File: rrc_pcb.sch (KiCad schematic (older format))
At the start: 10 parts, among them J1 Voltage Regulator Input, U1 ADXL357Z, U2 Teensy3.6-teensy, U3 BN220-GPS, U4 MS5611

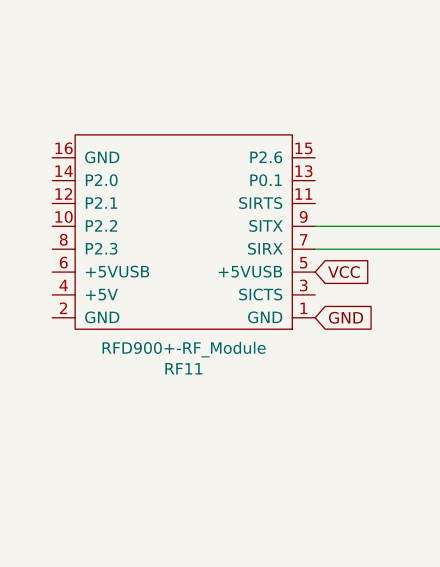
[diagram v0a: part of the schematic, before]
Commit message: added rfd v5-vusb jumper
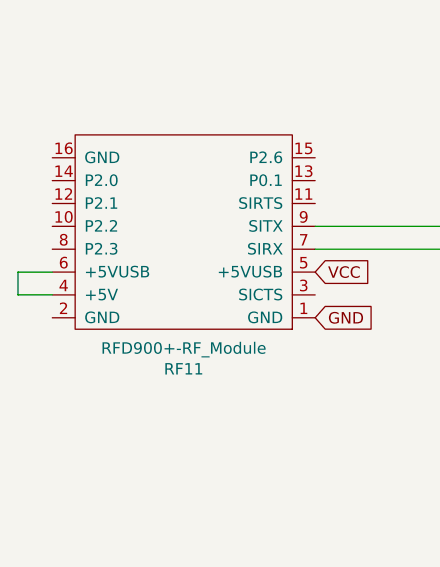
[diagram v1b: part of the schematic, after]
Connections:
- wire segments 38 -> 41
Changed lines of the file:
@@
 Wire Wire Line
 	10150 4900 10150 5300
+Wire Wire Line
+	1800 4600 1650 4600
+Wire Wire Line
+	1650 4600 1650 4500
+Wire Wire Line
+	1650 4500 1800 4500
 $EndSCHEMATC

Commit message: AC_added cool RRC logo
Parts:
- added U5: logo, logo:RRC_logo, symbol rrc_pcb-rescue:logo
- J1: symbol Connector:Conn_01x02_Male -> rrc_pcb-rescue:Conn_01x02_Male-Connector
- R1, R2, R3, R4: symbol Device:R -> rrc_pcb-rescue:R-Device
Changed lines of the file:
@@
 $EndComp
 $Comp
-L Device:R R4
+L rrc_pcb-rescue:R-Device R4
 U 1 1 60F41F75
 P 3200 2600
@@
 $EndComp
 $Comp
-L Device:R R3
+L rrc_pcb-rescue:R-Device R3
 U 1 1 60F426BB
 P 3200 2700
@@
 $EndComp
 $Comp
-L Device:R R1
+L rrc_pcb-rescue:R-Device R1
 U 1 1 60F42E96
 P 7800 4600
@@
 $EndComp
 $Comp
-L Device:R R2
+L rrc_pcb-rescue:R-Device R2
 U 1 1 60F4361A
 P 7800 5000
@@
 $EndComp
 $Comp
-L power:+5V #PWR01
+L rrc_pcb-rescue:+5V-power #PWR01
 U 1 1 60F4946E
 P 8700 1700
@@
 $EndComp
 $Comp
-L power:GND #PWR02
+L rrc_pcb-rescue:GND-power #PWR02
 U 1 1 60F49AB9
 P 8700 1800
@@
 $EndComp
 $Comp
-L Connector:Conn_01x02_Male J1
+L rrc_pcb-rescue:Conn_01x02_Male-Connector J1
 U 1 1 60F4B4B7
 P 8350 1700
@@
 Wire Wire Line
 	1650 4500 1800 4500
+$Comp
+L rrc_pcb-rescue:logo U5
+U 1 1 60F65807
+P 2100 7050
+F 0 "U5" H 2228 7071 50  0000 L CNN
+F 1 "logo" H 2228 6980 50  0000 L CNN
+F 2 "logo:RRC_logo" H 2100 7050 50  0001 C CNN
+F 3 "" H 2100 7050 50  0001 C CNN
+	1    2100 7050
+	1    0    0    -1
+$EndComp
 $EndSCHEMATC

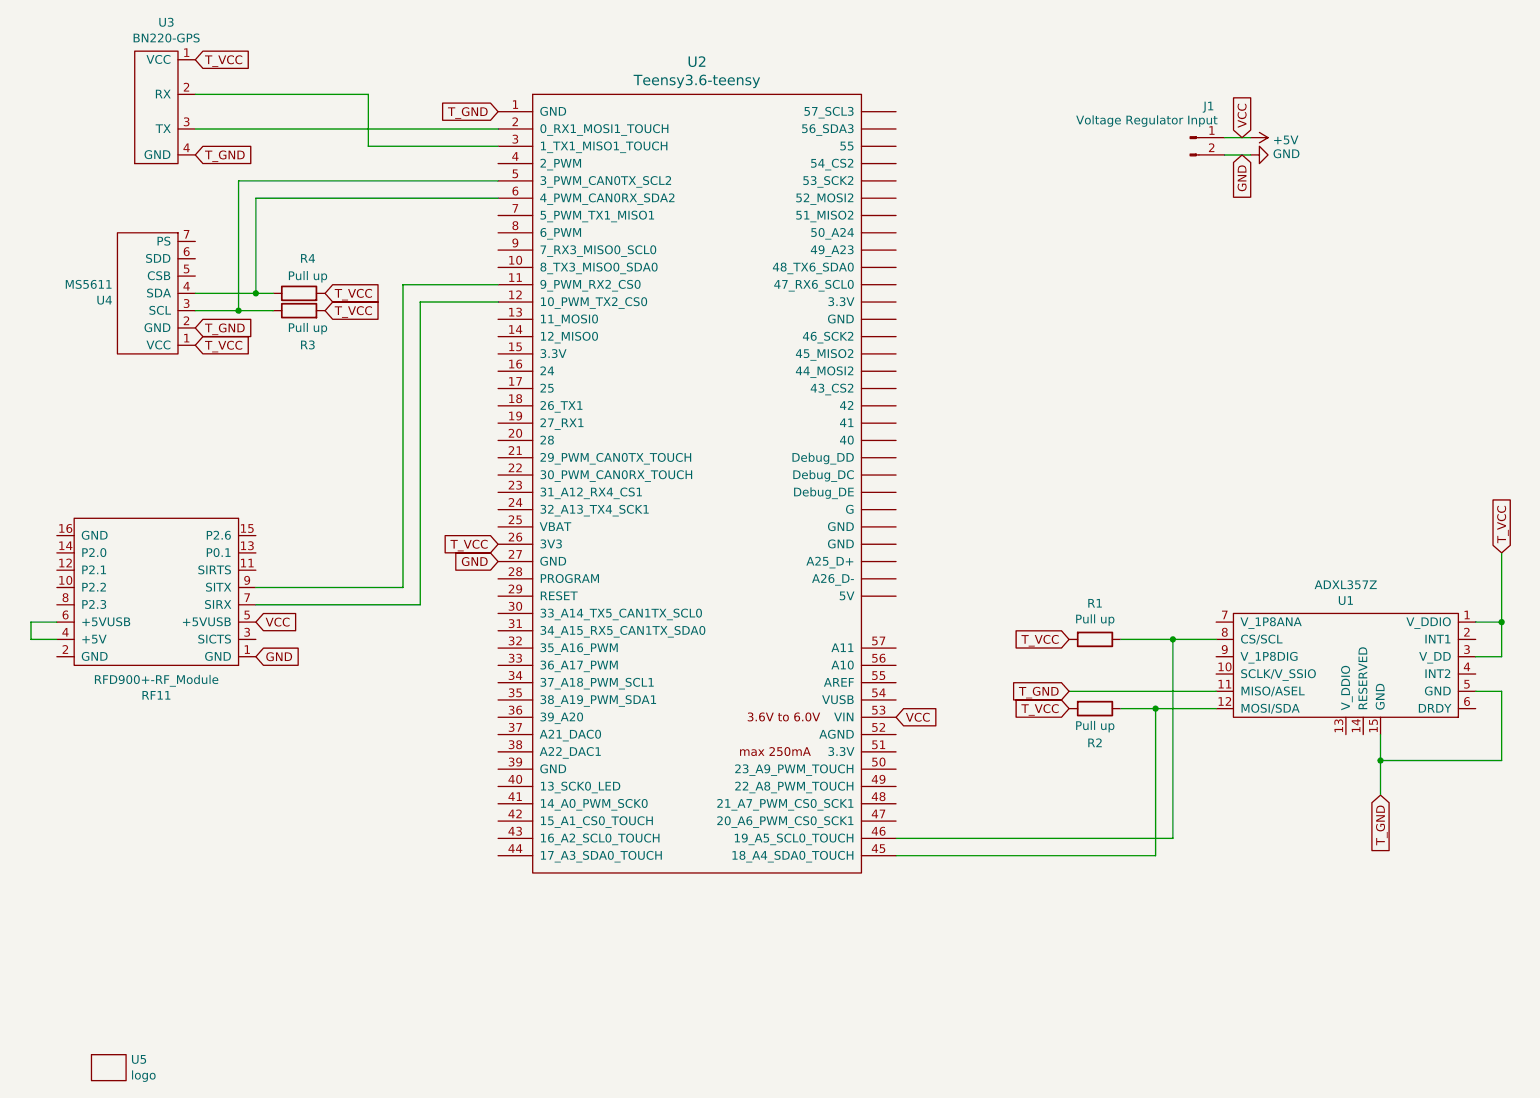
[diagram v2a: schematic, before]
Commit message: added buzzer
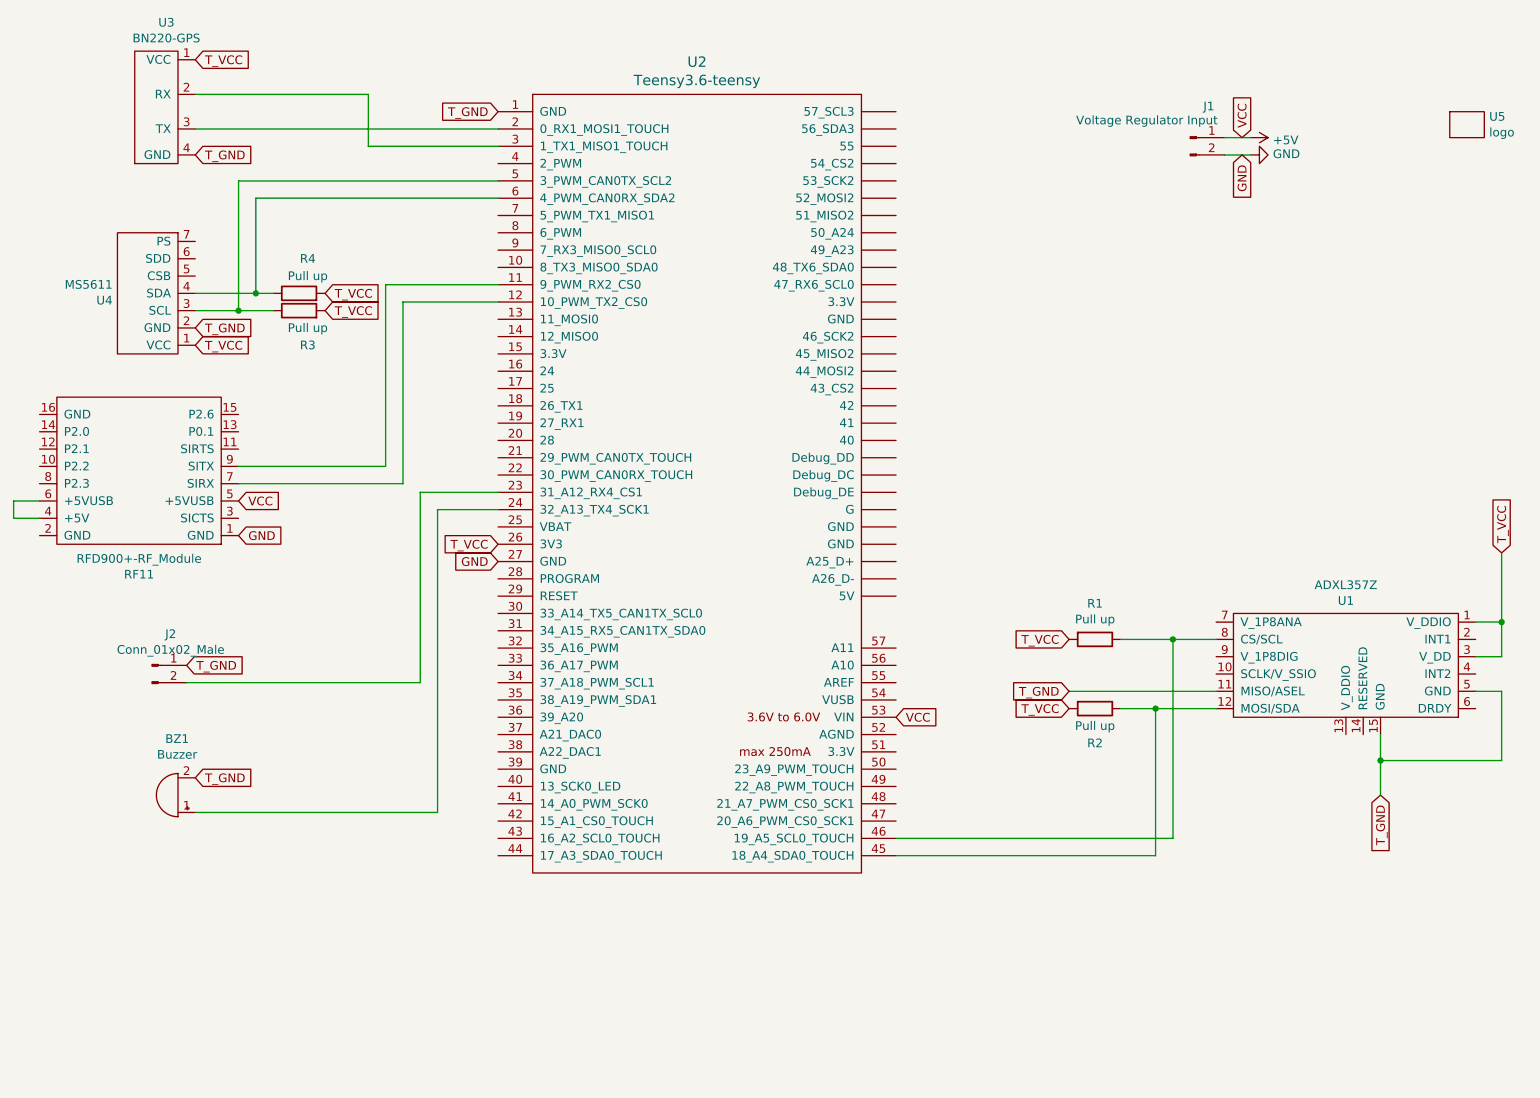
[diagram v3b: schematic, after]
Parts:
- added BZ1: Buzzer, Buzzer_Beeper:Buzzer_12x9.5RM7.6, symbol Device:Buzzer
- added J2: Conn_01x02_Male, Connector_PinHeader_2.54mm:PinHeader_1x02_P2.54mm_Vertical, symbol Connector:Conn_01x02_Male
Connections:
- net T_GND: now also BZ1.2 (+), J2.1 (Pin_1)
- net at U2.23 (31_A12_RX4_CS1): now also J2.2 (Pin_2)
- net at U2.24 (32_A13_TX4_SCK1): now also BZ1.1 (-)
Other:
- moved on the sheet: RF11, U5
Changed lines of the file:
@@
 L parts:RFD900+-RF_Module RF11
 U 1 1 60F3CA44
-P 2700 4700
-F 0 "RF11" H 3025 4925 50  0000 C CNN
-F 1 "RFD900+-RF_Module" H 3025 4834 50  0000 C CNN
-F 2 "rfd900+:RFD900+" H 2700 4700 50  0001 C CNN
-F 3 "" H 2700 4700 50  0001 C CNN
-	1    2700 4700
+P 2600 4000
+F 0 "RF11" H 2925 4225 50  0000 C CNN
+F 1 "RFD900+-RF_Module" H 2925 4134 50  0000 C CNN
+F 2 "rfd900+:RFD900+" H 2600 4000 50  0001 C CNN
+F 3 "" H 2600 4000 50  0001 C CNN
+	1    2600 4000
 	-1   0    0    1
 $EndComp
@@
 Text GLabel 2600 2900 2    50   Input ~ 0
 T_VCC
-Text GLabel 2950 4700 2    50   Input ~ 0
+Text GLabel 2850 4000 2    50   Input ~ 0
 GND
-Text GLabel 2950 4500 2    50   Input ~ 0
+Text GLabel 2850 3800 2    50   Input ~ 0
 VCC
 Wire Wire Line
-	2950 4400 3900 4400
-Wire Wire Line
-	3900 4400 3900 2650
-Wire Wire Line
-	3900 2650 4350 2650
-Wire Wire Line
-	2950 4300 3800 4300
-Wire Wire Line
-	3800 4300 3800 2550
-Wire Wire Line
-	3800 2550 4350 2550
+	2850 3700 3800 3700
+Wire Wire Line
+	2850 3600 3700 3600
 Wire Wire Line
 	2950 2600 2950 2050
@@
 	10150 4900 10150 5300
 Wire Wire Line
-	1800 4600 1650 4600
-Wire Wire Line
-	1650 4600 1650 4500
-Wire Wire Line
-	1650 4500 1800 4500
+	1700 3900 1550 3900
+Wire Wire Line
+	1550 3900 1550 3800
+Wire Wire Line
+	1550 3800 1700 3800
 $Comp
 L rrc_pcb-rescue:logo U5
 U 1 1 60F65807
-P 2100 7050
-F 0 "U5" H 2228 7071 50  0000 L CNN
-F 1 "logo" H 2228 6980 50  0000 L CNN
-F 2 "logo:RRC_logo" H 2100 7050 50  0001 C CNN
-F 3 "" H 2100 7050 50  0001 C CNN
-	1    2100 7050
+P 9950 1600
+F 0 "U5" H 10078 1621 50  0000 L CNN
+F 1 "logo" H 10078 1530 50  0000 L CNN
+F 2 "logo:RRC_logo" H 9950 1600 50  0001 C CNN
+F 3 "" H 9950 1600 50  0001 C CNN
+	1    9950 1600
 	1    0    0    -1
 $EndComp
+$Comp
+L Device:Buzzer BZ1
+U 1 1 60F65603
+P 2500 5500
+F 0 "BZ1" H 2505 5175 50  0000 C CNN
+F 1 "Buzzer" H 2505 5266 50  0000 C CNN
+F 2 "Buzzer_Beeper:Buzzer_12x9.5RM7.6" V 2475 5600 50  0001 C CNN
+F 3 "~" V 2475 5600 50  0001 C CNN
+	1    2500 5500
+	-1   0    0    1
+$EndComp
+$Comp
+L Connector:Conn_01x02_Male J2
+U 1 1 60F67653
+P 2350 4750
+F 0 "J2" H 2458 4931 50  0000 C CNN
+F 1 "Conn_01x02_Male" H 2458 4840 50  0000 C CNN
+F 2 "Connector_PinHeader_2.54mm:PinHeader_1x02_P2.54mm_Vertical" H 2350 4750 50  0001 C CNN
+F 3 "~" H 2350 4750 50  0001 C CNN
+	1    2350 4750
+	1    0    0    -1
+$EndComp
+Text GLabel 2600 5400 2    50   Input ~ 0
+T_GND
+Text GLabel 2550 4750 2    50   Input ~ 0
+T_GND
+Wire Wire Line
+	3700 3600 3700 2550
+Wire Wire Line
+	3800 3700 3800 2650
+Wire Wire Line
+	3800 2650 4350 2650
+Wire Wire Line
+	3700 2550 4350 2550
+Wire Wire Line
+	2550 4850 3900 4850
+Wire Wire Line
+	3900 4850 3900 3750
+Wire Wire Line
+	3900 3750 4350 3750
+Wire Wire Line
+	2600 5600 4000 5600
+Wire Wire Line
+	4000 5600 4000 3850
+Wire Wire Line
+	4000 3850 4350 3850
 $EndSCHEMATC

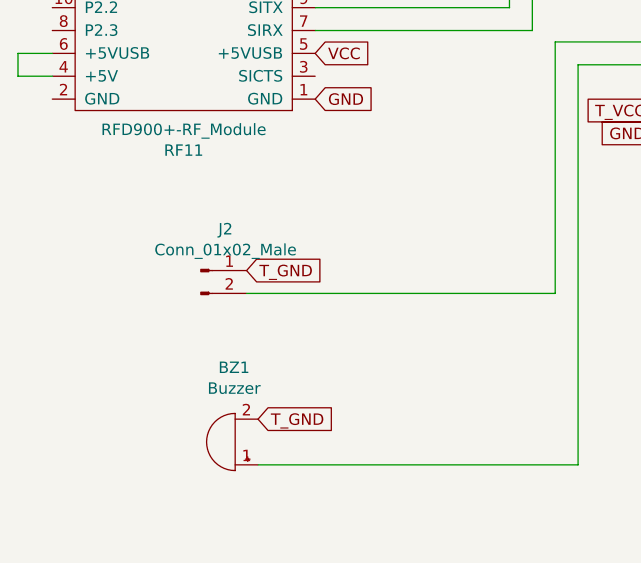
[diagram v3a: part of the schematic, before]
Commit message: added buzzer enable pin
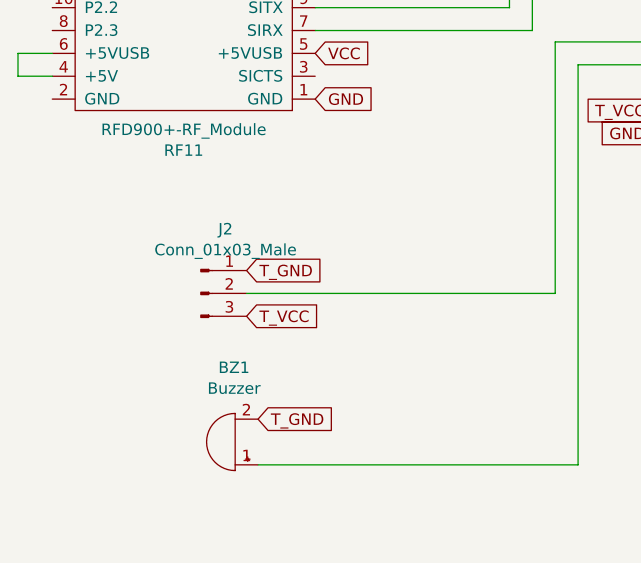
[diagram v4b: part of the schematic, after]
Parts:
- removed J2: Conn_01x02_Male, Connector_PinHeader_2.54mm:PinHeader_1x02_P2.54mm_Vertical, symbol Connector:Conn_01x02_Male
- added J2: Conn_01x03_Male, Connector_PinHeader_2.54mm:PinHeader_1x03_P2.54mm_Vertical, symbol Connector:Conn_01x03_Male
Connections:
- net T_GND: now also J2.1 (Pin_1)
- net T_VCC: now also J2.3 (Pin_3)
- net at U2.23 (31_A12_RX4_CS1): now also J2.2 (Pin_2)
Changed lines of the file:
@@
 	-1   0    0    1
-$EndComp
-$Comp
-L Connector:Conn_01x02_Male J2
-U 1 1 60F67653
-P 2350 4750
-F 0 "J2" H 2458 4931 50  0000 C CNN
-F 1 "Conn_01x02_Male" H 2458 4840 50  0000 C CNN
-F 2 "Connector_PinHeader_2.54mm:PinHeader_1x02_P2.54mm_Vertical" H 2350 4750 50  0001 C CNN
-F 3 "~" H 2350 4750 50  0001 C CNN
-	1    2350 4750
-	1    0    0    -1
 $EndComp
 Text GLabel 2600 5400 2    50   Input ~ 0
@@
 Wire Wire Line
 	4000 3850 4350 3850
+$Comp
+L Connector:Conn_01x03_Male J2
+U 1 1 60F65D90
+P 2350 4850
+F 0 "J2" H 2458 5131 50  0000 C CNN
+F 1 "Conn_01x03_Male" H 2458 5040 50  0000 C CNN
+F 2 "Connector_PinHeader_2.54mm:PinHeader_1x03_P2.54mm_Vertical" H 2350 4850 50  0001 C CNN
+F 3 "~" H 2350 4850 50  0001 C CNN
+	1    2350 4850
+	1    0    0    -1
+$EndComp
+Text GLabel 2550 4950 2    50   Input ~ 0
+T_VCC
 $EndSCHEMATC

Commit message: moved standoffs around for better placement structurally , PCB is ready to go
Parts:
- BZ1: symbol Device:Buzzer -> rrc_pcb-rescue:Buzzer-Device
- J2: symbol Connector:Conn_01x03_Male -> rrc_pcb-rescue:Conn_01x03_Male-Connector
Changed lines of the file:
@@
 $EndComp
 $Comp
-L Device:Buzzer BZ1
+L rrc_pcb-rescue:Buzzer-Device BZ1
 U 1 1 60F65603
 P 2500 5500
@@
 	4000 3850 4350 3850
 $Comp
-L Connector:Conn_01x03_Male J2
+L rrc_pcb-rescue:Conn_01x03_Male-Connector J2
 U 1 1 60F65D90
 P 2350 4850

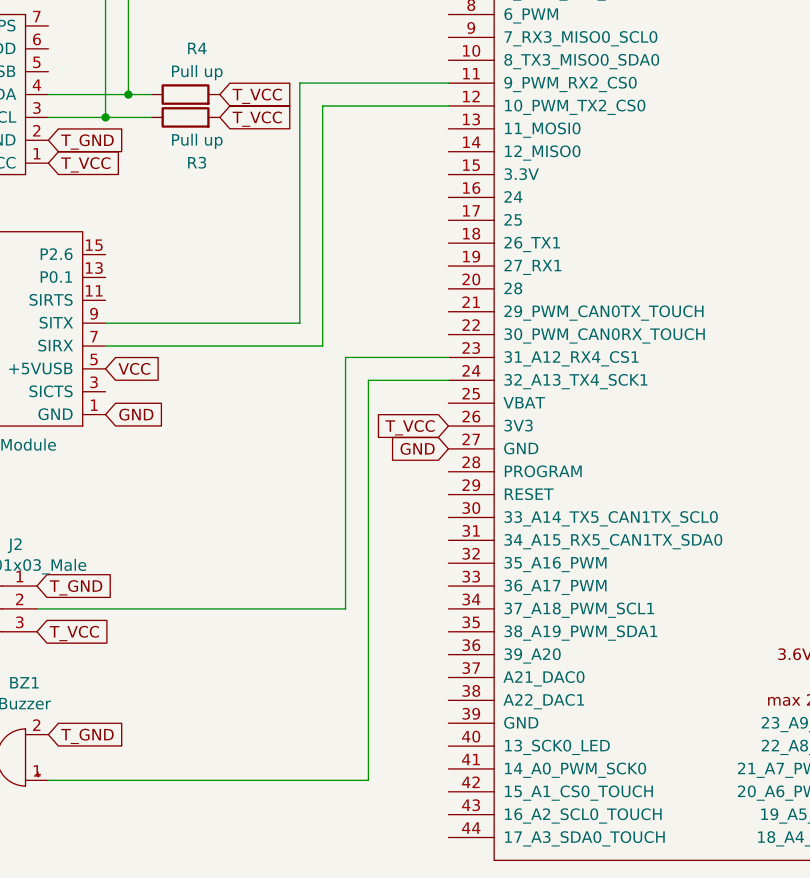
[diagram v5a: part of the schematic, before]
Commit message: fixed prototype mistakes
changed some drill holes positions
changed GPS connector
changed teensy used pins
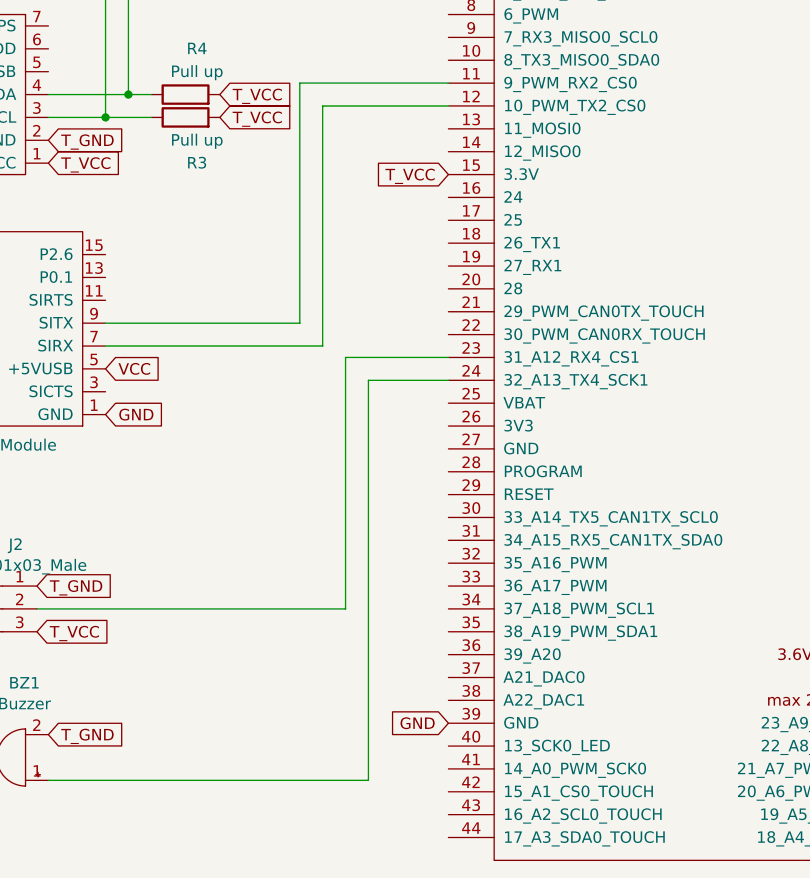
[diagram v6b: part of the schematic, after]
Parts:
- U3: footprint Connector_JST:JST_SH_BM04B-SRSS-TB_1x04-1MP_P1.00mm_Vertical -> Connector_PinHeader_2.54mm:PinHeader_1x04_P2.54mm_Horizontal
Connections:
- net GND: now also U2.39 (GND); no longer U2.27 (GND)
- net T_VCC: now also U2.15 (3.3V); no longer U2.26 (3V3)
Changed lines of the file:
@@
 F 0 "U3" V 2915 1517 50  0000 C CNN
 F 1 "BN220-GPS" V 2824 1517 50  0000 C CNN
-F 2 "Connector_JST:JST_SH_BM04B-SRSS-TB_1x04-1MP_P1.00mm_Vertical" H 2400 1550 50  0001 C CNN
+F 2 "Connector_PinHeader_2.54mm:PinHeader_1x04_P2.54mm_Horizontal" H 2400 1550 50  0001 C CNN
 F 3 "" H 2400 1550 50  0001 C CNN
 	1    2400 1550
@@
 Text GLabel 6650 5050 2    50   Input ~ 0
 VCC
-Text GLabel 4350 4050 0    50   Input ~ 0
+Text GLabel 4350 2950 0    50   Input ~ 0
 T_VCC
 Text GLabel 2600 1250 2    50   Input ~ 0
@@
 Wire Wire Line
 	8250 4600 8500 4600
-Text GLabel 4350 4150 0    50   Input ~ 0
+Text GLabel 4350 5350 0    50   Input ~ 0
 GND
 Wire Wire Line
